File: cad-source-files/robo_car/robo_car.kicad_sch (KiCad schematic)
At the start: 85 parts, among them J1 Conn_01x06_MountingPin, J16 Conn_01x02_MountingPin, J2 ftdi_conn, J3 Conn_01x06_MountingPin, J4 Conn_01x04, J5 Conn_01x04, J6 Conn_01x06_MountingPin, J7 Conn_01x02_MountingPin, J8 Conn_01x02_MountingPin, SW1 SW_Push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

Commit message: move Olivia's stuffy stuff to the correct repo
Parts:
- removed D7: D_TVS_x2_AAC, Package_TO_SOT_SMD:SOT-23, symbol Device:D_TVS_x2_AAC
- removed J4: Conn_01x04, Connector_JST:JST_PH_B4B-PH-SM4-TB_1x04-1MP_P2.00mm_Vertical, symbol Connector_Generic_MountingPin:Conn_01x04_MountingPin
- removed J5: Conn_01x04, Connector_JST:JST_PH_S4B-PH-SM4-TB_1x04-1MP_P2.00mm_Horizontal, symbol Connector_Generic_MountingPin:Conn_01x04_MountingPin
- removed U5: Trans_CAN_SN65HVD230DR, Package_SO:CAN-TRANS-SN65HVD230DR, symbol Evezor_Library:Trans_CAN_SN65HVD230DR
- added C16: 22uF, Capacitor_SMD:C_0805_2012Metric, symbol Device:C_Small
- added H28, H29: MountingHole, MountingHole:MountingHole_3.2mm_M3_ISO14580, symbol Mechanical:MountingHole
- added J4: Barrel_Jack, Connector_BarrelJack:BarrelJack_Horizontal, symbol Connector:Barrel_Jack
- added J5: Conn_01x04, Connector_PinSocket_2.54mm:PinSocket_1x04_P2.54mm_Vertical, symbol Connector_Generic:Conn_01x04
- C14: value .1uF -> 22uF; footprint Capacitor_SMD:C_0603_1608Metric -> Capacitor_SMD:C_0805_2012Metric
- J2: footprint Connector_JST:JST_SH_BM06B-SRSS-TB_1x06-1MP_P1.00mm_Vertical -> Connector_JST:JST_SH_SM06B-SRSS-TB_1x06-1MP_P1.00mm_Horizontal
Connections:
- net CAN_RX is gone; now on net INPUT_A: U3.27 (IO16)
- net CAN_TX is gone; now on net INPUT_C: U3.26 (A2-IO4)
- net +3V3: now also J5.1 (Pin_1); no longer C15.1
- net GND: now also C16.2, J4.2, J5.2 (Pin_2)
- net INPUT_A: no longer U3.29 (IO5)
- net INPUT_B: now also U3.28 (IO17); no longer U3.30 (SCL0-VCLK-IO18)
- net INPUT_C: no longer U3.28 (IO17)
- net SCL: now also U3.31 (SDA0-VMISO-IO19); no longer U3.36 (IO22)
- net SDA: now also U3.33 (IO21); no longer U3.37 (VMOSI-IO23)
- net SERVO_0: now also U3.30 (SCL0-VCLK-IO18); no longer U3.33 (IO21)
- net SERVO_1: now also U3.29 (IO5); no longer U3.31 (SDA0-VMISO-IO19)
- net VBUS: now also J4.1
- net VREG_OUT: now also C15.1, C16.1
- new net LCD_SCL: J5.3 (Pin_3), U3.36 (IO22)
- new net LCD_SDA: J5.4 (Pin_4), U3.37 (VMOSI-IO23)
- no-connect marks 9 -> 8

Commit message: Still gotta fix the Angie zong shtuff but thats mostly it
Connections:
- net VBUS: no longer J2.5 (Pin_5)
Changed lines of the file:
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@@
-    (pin "1")
-  )
-  (symbol (lib_id "power:VBUS") (at 394.97 170.18 90) (unit 1)
-    (in_bom yes) (on_board yes)
-    (property "Reference" "#PWR0112" (id 0) (at 398.78 170.18 0)
-      (effects (font (size 1.27 1.27)) hide)
-    )
-    (property "Value" "VBUS" (id 1) (at 389.89 170.18 90))
-    (property "Footprint" "" (id 2) (at 394.97 170.18 0)
-      (effects (font (size 1.27 1.27)) hide)
-    )
-    (property "Datasheet" "" (id 3) (at 394.97 170.18 0)
-      (effects (font (size 1.27 1.27)) hide)
-    )
     (pin "1")
   )
@@
       (reference "#PWR0110") (unit 1) (value "GND") (footprint "")
     )
-    (path "/00000000-0000-0000-0000-000060c4783e"
-      (reference "#PWR0112") (unit 1) (value "VBUS") (footprint "")
-    )
     (path "/00000000-0000-0000-0000-00006092222d"

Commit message: 3rd try lets go
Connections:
- net INPUT_A renamed IO16
- net INPUT_B renamed IO17
- net INPUT_C renamed IO4
- net INPUT_D renamed IO13
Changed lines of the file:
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@@
     (effects (font (size 1.27 1.27)) (justify right bottom))
   )
-  (label "INPUT_C" (at 41.91 129.54 0)
+  (label "IO4" (at 41.91 129.54 0)
     (effects (font (size 1.27 1.27)) (justify left bottom))
   )
@@
     (effects (font (size 1.27 1.27)) (justify right bottom))
   )
-  (label "INPUT_C" (at 311.15 152.4 180)
+  (label "IO4" (at 311.15 152.4 180)
     (effects (font (size 1.27 1.27)) (justify right bottom))
   )
@@
     (effects (font (size 1.27 1.27)) (justify left bottom))
   )
-  (label "INPUT_A" (at 41.91 127 0)
+  (label "IO16" (at 41.91 127 0)
     (effects (font (size 1.27 1.27)) (justify left bottom))
   )
@@
     (effects (font (size 1.27 1.27)) (justify left bottom))
   )
-  (label "INPUT_B" (at 316.23 170.18 180)
+  (label "IO17" (at 316.23 170.18 180)
     (effects (font (size 1.27 1.27)) (justify right bottom))
   )
@@
     (effects (font (size 1.27 1.27)) (justify right bottom))
   )
-  (label "INPUT_D" (at 314.96 160.02 180)
+  (label "IO13" (at 314.96 160.02 180)
     (effects (font (size 1.27 1.27)) (justify right bottom))
   )
@@
     (effects (font (size 1.27 1.27)) (justify right bottom))
   )
-  (label "INPUT_B" (at 41.91 124.46 0)
+  (label "IO17" (at 41.91 124.46 0)
     (effects (font (size 1.27 1.27)) (justify left bottom))
   )
-  (label "INPUT_A" (at 311.15 167.64 180)
+  (label "IO16" (at 311.15 167.64 180)
     (effects (font (size 1.27 1.27)) (justify right bottom))
   )
@@
     (effects (font (size 1.27 1.27)) (justify left bottom))
   )
-  (label "INPUT_D" (at 41.91 121.92 0)
+  (label "IO13" (at 41.91 121.92 0)
     (effects (font (size 1.27 1.27)) (justify left bottom))
   )

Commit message: ok NOW its done
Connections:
- net ANALOG_A renamed IO39
- net ANALOG_B renamed IO34
- net ANALOG_C renamed IO35
- net ANALOG_D renamed IO32
- net CAN_SLP: no longer names the net of U3.24 (LOW@BOOT-A2-IO2)
- net SCL renamed IO19
- net SDA renamed IO21
- net SERVO_0 renamed IO18
- net SERVO_1 renamed IO5
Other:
- note removed: "*"
- moved on the sheet: J1, J3, J6

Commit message: gettin down with the qwiic-ness
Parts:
- added J9: Conn_01x02_MountingPin, Connector_JST:JST_XH_2_VERTICAL, symbol Connector_Generic_MountingPin:Conn_01x02_MountingPin
- added SW3: SW_SPDT, Button_Switch_THT:SW_SLIDE_SS-12D10L9, symbol Switch:SW_SPDT
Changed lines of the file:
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@@
     )
+  )
+  (symbol (lib_id "Connector_Generic_MountingPin:Conn_01x02_MountingPin") (at 261.62 30.48 90) (unit 1)
+    (in_bom yes) (on_board yes)
+    (property "Reference" "J9" (id 0) (at 258.9335 31.6229 0)
+      (effects (font (size 1.27 1.27)) (justify left))
+    )
+    (property "Value" "Conn_01x02_MountingPin" (id 1) (at 271.8686 27.8129 90)
+      (effects (font (size 0.75 0.75)) (justify left))
+    )
+    (property "Footprint" "Connector_JST:JST_XH_2_VERTICAL" (id 2) (at 261.62 30.48 0)
+      (effects (font (size 1.27 1.27)) hide)
+    )
+    (property "Datasheet" "~" (id 3) (at 261.62 30.48 0)
+      (effects (font (size 1.27 1.27)) hide)
+    )
+    (pin "1")
+    (pin "2")
+    (pin "MP")
   )
   (symbol (lib_id "power:GND") (at 86.36 237.49 0) (mirror y) (unit 1)
@@
     (pin "2")
   )
+  (symbol (lib_id "Switch:SW_SPDT") (at 279.4 35.56 0) (unit 1)
+    (in_bom yes) (on_board yes) (fields_autoplaced)
+    (property "Reference" "SW3" (id 0) (at 279.4 27.94 0))
+    (property "Value" "SW_SPDT" (id 1) (at 279.4 30.48 0))
+    (property "Footprint" "Button_Switch_THT:SW_SLIDE_SS-12D10L9" (id 2) (at 279.4 35.56 0)
+      (effects (font (size 1.27 1.27)) hide)
+    )
+    (property "Datasheet" "~" (id 3) (at 279.4 35.56 0)
+      (effects (font (size 1.27 1.27)) hide)
+    )
+    (pin "1")
+    (pin "2")
+    (pin "3")
+  )
   (symbol (lib_id "Device:C_Small") (at 102.87 218.44 180) (unit 1)
     (in_bom yes) (on_board yes)
@@
       (reference "J8") (unit 1) (value "Conn_01x02_MountingPin") (footprint "Connector_JST:JST_XH_2_VERTICAL")
     )
+    (path "/973dd881-85aa-4ef4-886b-98d3b7b12937"
+      (reference "J9") (unit 1) (value "Conn_01x02_MountingPin") (footprint "Connector_JST:JST_XH_2_VERTICAL")
+    )
     (path "/faf4ae82-075b-4bb3-a263-db50304d39f6"
       (reference "J16") (unit 1) (value "Conn_01x02_MountingPin") (footprint "Connector_JST:JST_XH_2_VERTICAL")
@@
       (reference "SW2") (unit 1) (value "SW_Push") (footprint "Button_Switch_SMD:SWITCH_2x3_SMD_TACTILE_GREEN")
     )
+    (path "/d0e74642-b451-4818-8635-6c6460d97fb7"
+      (reference "SW3") (unit 1) (value "SW_SPDT") (footprint "Button_Switch_THT:SW_SLIDE_SS-12D10L9")
+    )
     (path "/fff19411-e711-4d7a-b087-47ee0969128e"

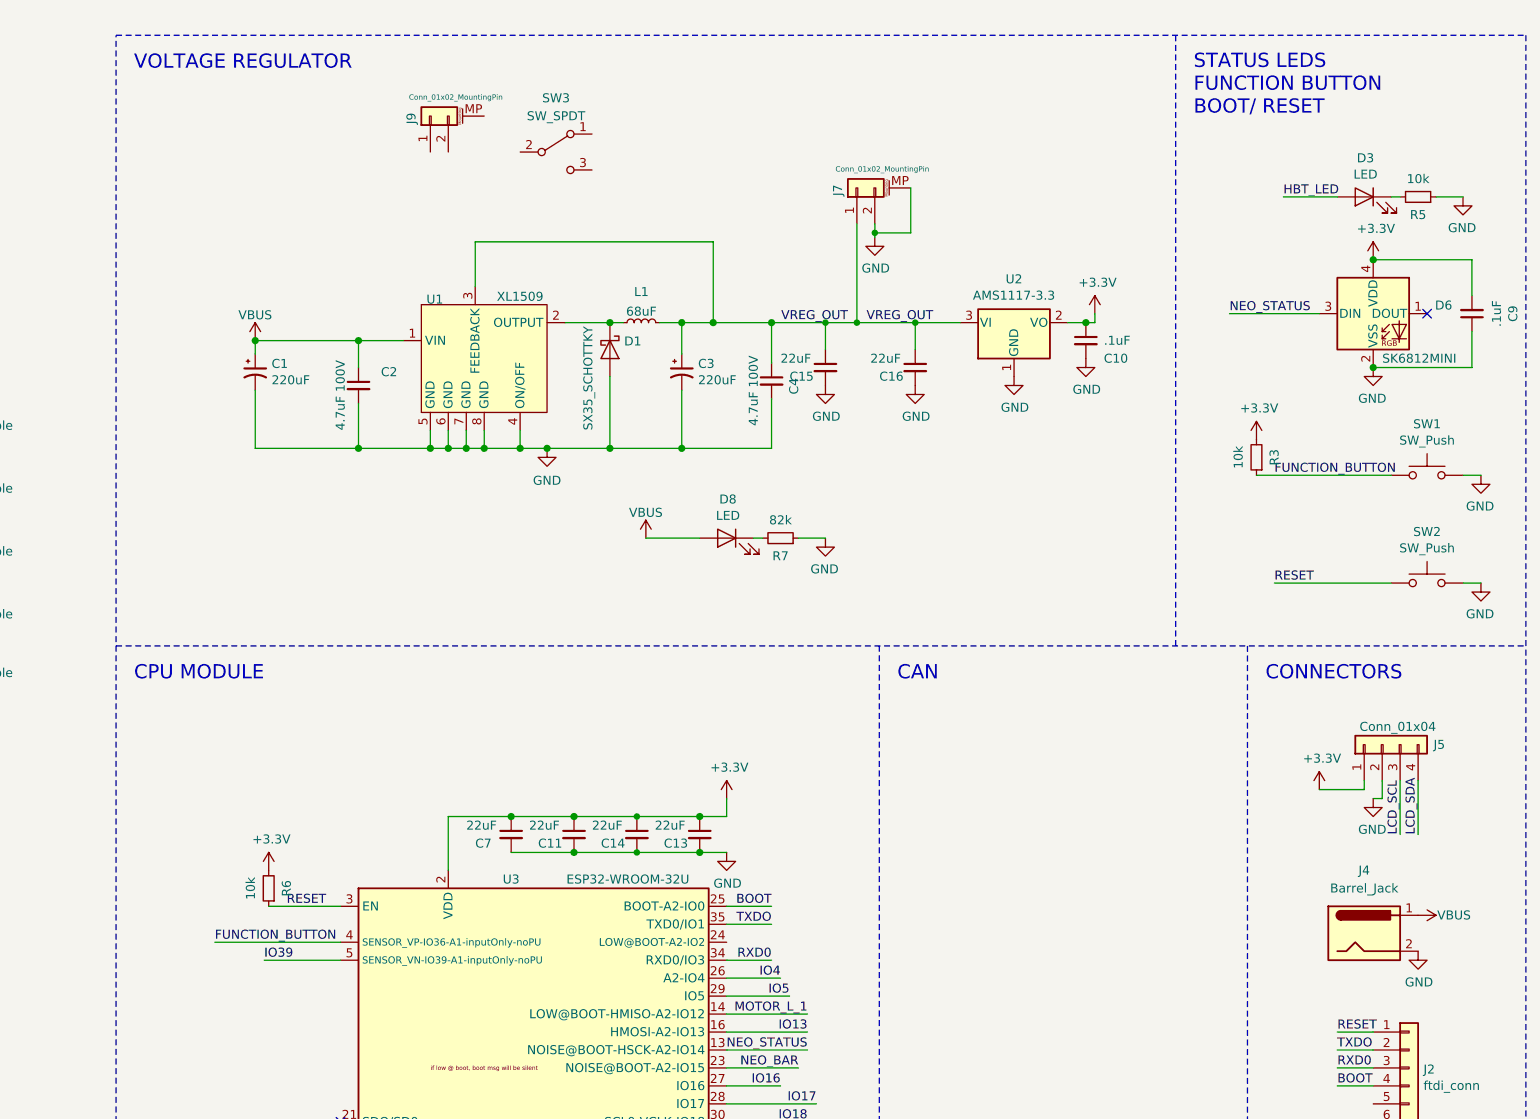
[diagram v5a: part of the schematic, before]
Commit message: mo 4 has spawned
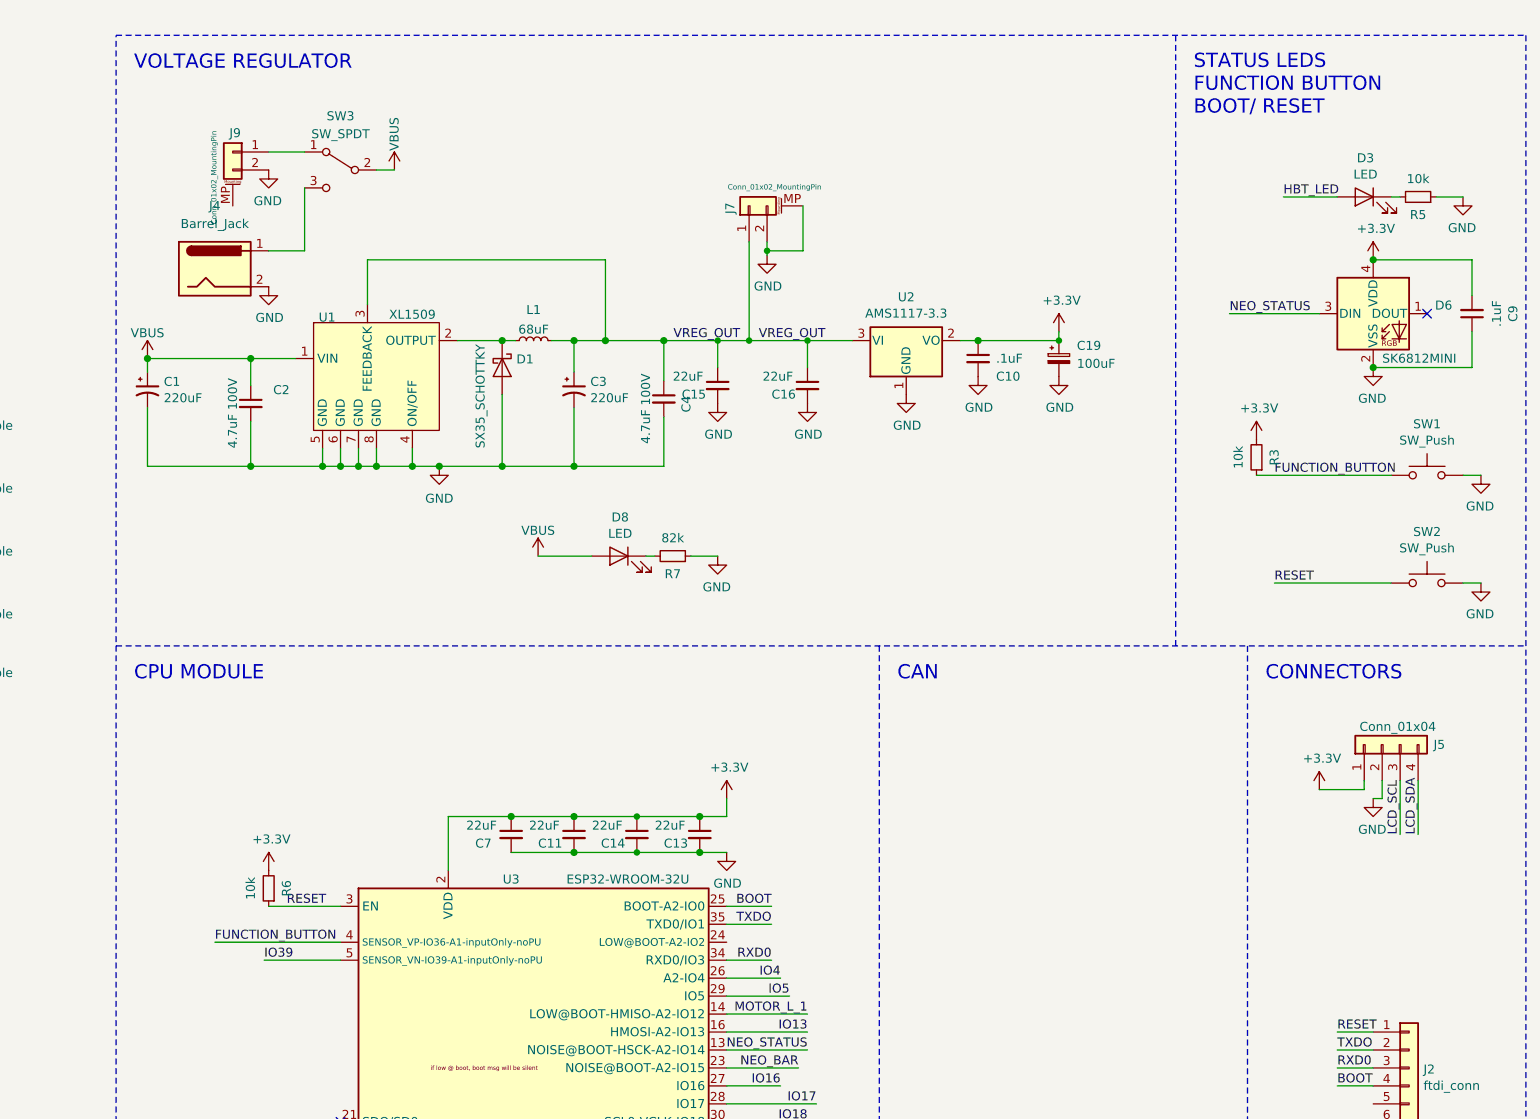
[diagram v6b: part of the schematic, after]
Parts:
- added C19: 100uF, Capacitor_Tantalum_SMD:CP_EIA-3528-21_Kemet-B, symbol Device:C_Polarized_Small
- J16, J8: footprint Connector_JST:JST_XH_2_VERTICAL -> Connector_JST:JST_PH_S2B-PH-K_1x02_P2.00mm_Horizontal
- J7: footprint Connector_JST:JST_XH_2_VERTICAL -> Connector_JST:JST_PH_B2B-PH-K_1x02_P2.00mm_Vertical
- J9: footprint Connector_JST:JST_XH_2_VERTICAL -> Connector_JST:JST_XH_B2B-XH-AM_1x02_P2.50mm_Vertical
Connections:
- net +3V3: now also C19.1
- net GND: now also J9.2 (Pin_2), C19.2
- net VBUS: now also SW3.2 (B); no longer J4.1
- net at J9.1 (Pin_1): now also SW3.1 (A)
- net at SW3.3 (C): now also J4.1
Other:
- moved on the sheet: C1, C10, C15, C16, C2, C3, C4, D1, D8, J4, J7, J9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
